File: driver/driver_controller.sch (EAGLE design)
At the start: 36 parts, among them IC1 FT232RL, U1 STM32F10XRXT6

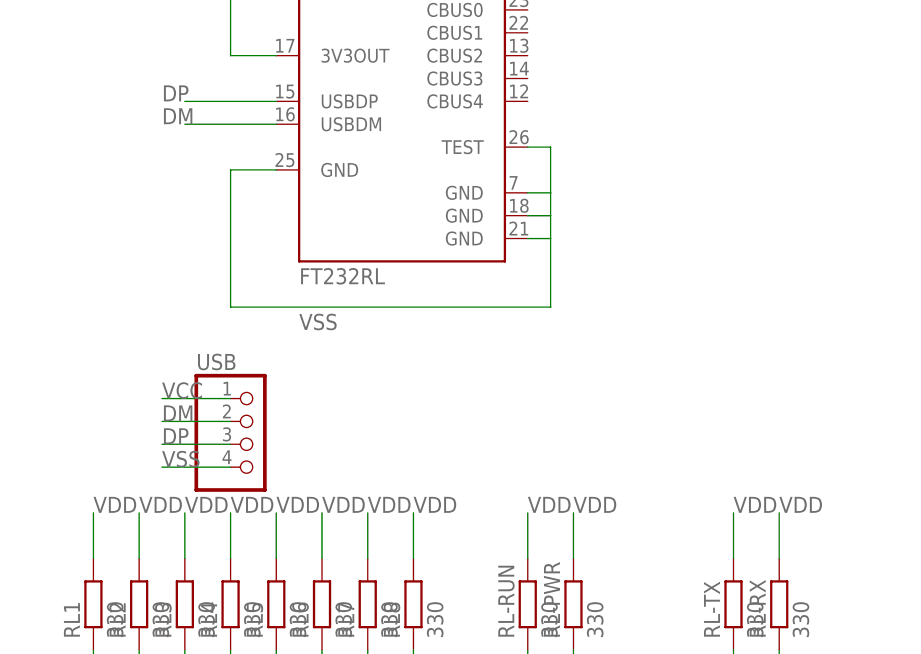
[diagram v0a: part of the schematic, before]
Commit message: ganti pake mini USB
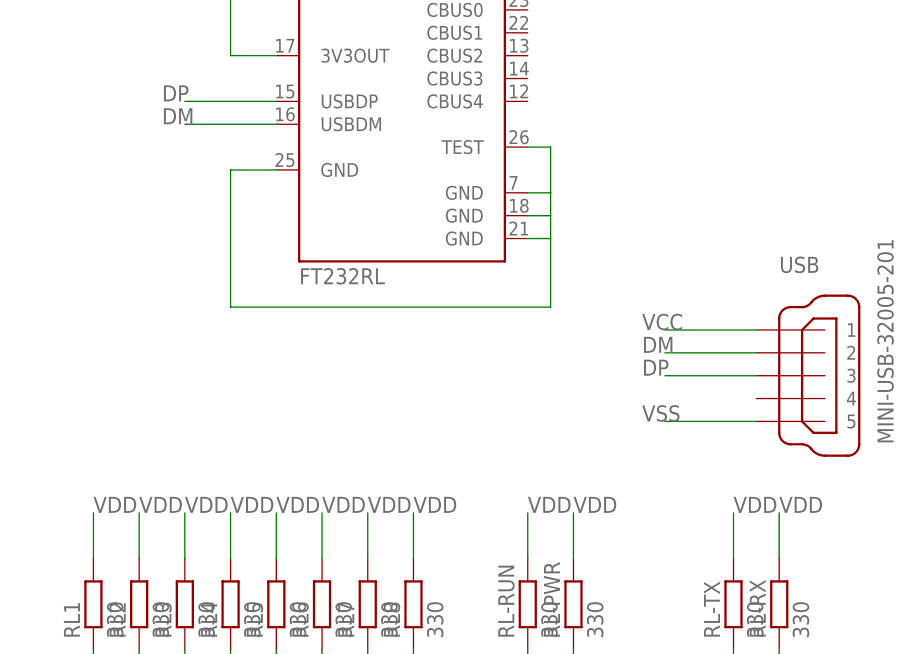
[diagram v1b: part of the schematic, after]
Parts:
- USB: value (none) -> MINI-USB-32005-201; device pinhead:PINHD-1X4 -> con-cypressindustries:MINI-USB-32005-201
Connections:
- net VSS: now also USB.5; no longer USB.4
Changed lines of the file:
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@@
 <part name="C-XA-1" library="resistor" deviceset="C-EU" device="C1206" value="22p"/>
 <part name="C-XA-2" library="resistor" deviceset="C-EU" device="C1206" value="22p"/>
-<part name="USB" library="pinhead" deviceset="PINHD-1X4" device=""/>
 <part name="RL1" library="resistor" deviceset="R-EU_" device="R1206" value="330"/>
 <part name="LED1" library="led" deviceset="LED" device="SML1206"/>
@@
 <part name="RL-RX" library="resistor" deviceset="R-EU_" device="R1206" value="330"/>
 <part name="L-RX" library="led" deviceset="LED" device="SML1206"/>
+<part name="USB" library="con-cypressindustries" deviceset="MINI-USB-" device="32005-201"/>
 </parts>
 <sheets>
@@
 <instance part="C-XA-1" gate="G$1" x="78.74" y="33.02" rot="R90"/>
 <instance part="C-XA-2" gate="G$1" x="78.74" y="27.94" rot="R90"/>
-<instance part="USB" gate="A" x="129.54" y="10.16"/>
 <instance part="RL1" gate="G$1" x="111.76" y="-7.62" rot="R90"/>
 <instance part="LED1" gate="G$1" x="111.76" y="-17.78"/>
@@
 <instance part="RL-RX" gate="G$1" x="187.96" y="-7.62" rot="R90"/>
 <instance part="L-RX" gate="G$1" x="187.96" y="-17.78"/>
+<instance part="USB" gate="G$1" x="190.5" y="17.78"/>
 </instances>
 <busses>
@@
 <pinref part="IC1" gate="1" pin="GND@2"/>
 <wire x1="160.02" y1="33.02" x2="162.56" y2="33.02" width="0.1524" layer="91"/>
-<label x="134.62" y="22.86" size="1.778" layer="95"/>
-</segment>
-<segment>
-<pinref part="USB" gate="A" pin="4"/>
-<wire x1="127" y1="7.62" x2="119.38" y2="7.62" width="0.1524" layer="91"/>
-<label x="119.38" y="7.62" size="1.778" layer="95"/>
 </segment>
 <segment>
@@
 <wire x1="165.1" y1="-22.86" x2="165.1" y2="-27.94" width="0.1524" layer="91"/>
 <label x="165.1" y="-27.94" size="1.778" layer="95"/>
+</segment>
+<segment>
+<pinref part="USB" gate="G$1" pin="5"/>
+<wire x1="185.42" y1="12.7" x2="175.26" y2="12.7" width="0.1524" layer="91"/>
+<label x="172.72" y="12.7" size="1.778" layer="95"/>
 </segment>
 </net>
@@
 </segment>
 <segment>
-<pinref part="USB" gate="A" pin="1"/>
-<wire x1="127" y1="15.24" x2="119.38" y2="15.24" width="0.1524" layer="91"/>
-<label x="119.38" y="15.24" size="1.778" layer="95"/>
-</segment>
-<segment>
 <pinref part="PWR" gate="-3" pin="KL"/>
 <wire x1="119.38" y1="-50.8" x2="111.76" y2="-50.8" width="0.1524" layer="91"/>
 <label x="111.76" y="-50.8" size="1.778" layer="95"/>
 </segment>
+<segment>
+<pinref part="USB" gate="G$1" pin="1"/>
+<wire x1="185.42" y1="22.86" x2="175.26" y2="22.86" width="0.1524" layer="91"/>
+<label x="172.72" y="22.86" size="1.778" layer="95"/>
+</segment>
 </net>
 <net name="DP" class="0">
@@
 </segment>
 <segment>
-<pinref part="USB" gate="A" pin="3"/>
-<wire x1="127" y1="10.16" x2="119.38" y2="10.16" width="0.1524" layer="91"/>
-<label x="119.38" y="10.16" size="1.778" layer="95"/>
+<pinref part="USB" gate="G$1" pin="3"/>
+<wire x1="185.42" y1="17.78" x2="175.26" y2="17.78" width="0.1524" layer="91"/>
+<label x="172.72" y="17.78" size="1.778" layer="95"/>
 </segment>
 </net>
@@
 </segment>
 <segment>
-<pinref part="USB" gate="A" pin="2"/>
-<wire x1="127" y1="12.7" x2="119.38" y2="12.7" width="0.1524" layer="91"/>
-<label x="119.38" y="12.7" size="1.778" layer="95"/>
-</segment>
-</net>
+<pinref part="USB" gate="G$1" pin="2"/>
+<wire x1="185.42" y1="20.32" x2="175.26" y2="20.32" width="0.1524" layer="91"/>
+<label x="172.72" y="20.32" size="1.778" layer="95"/>
+</segment>
+</net>
